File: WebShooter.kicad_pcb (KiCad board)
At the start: 2 copper layers, 60 x 46 mm, 29 parts, among them J1 ESP32_LEFT, J2 ESP32_RIGHT, Q1 AO3400A, U1 AMS1117-3.3

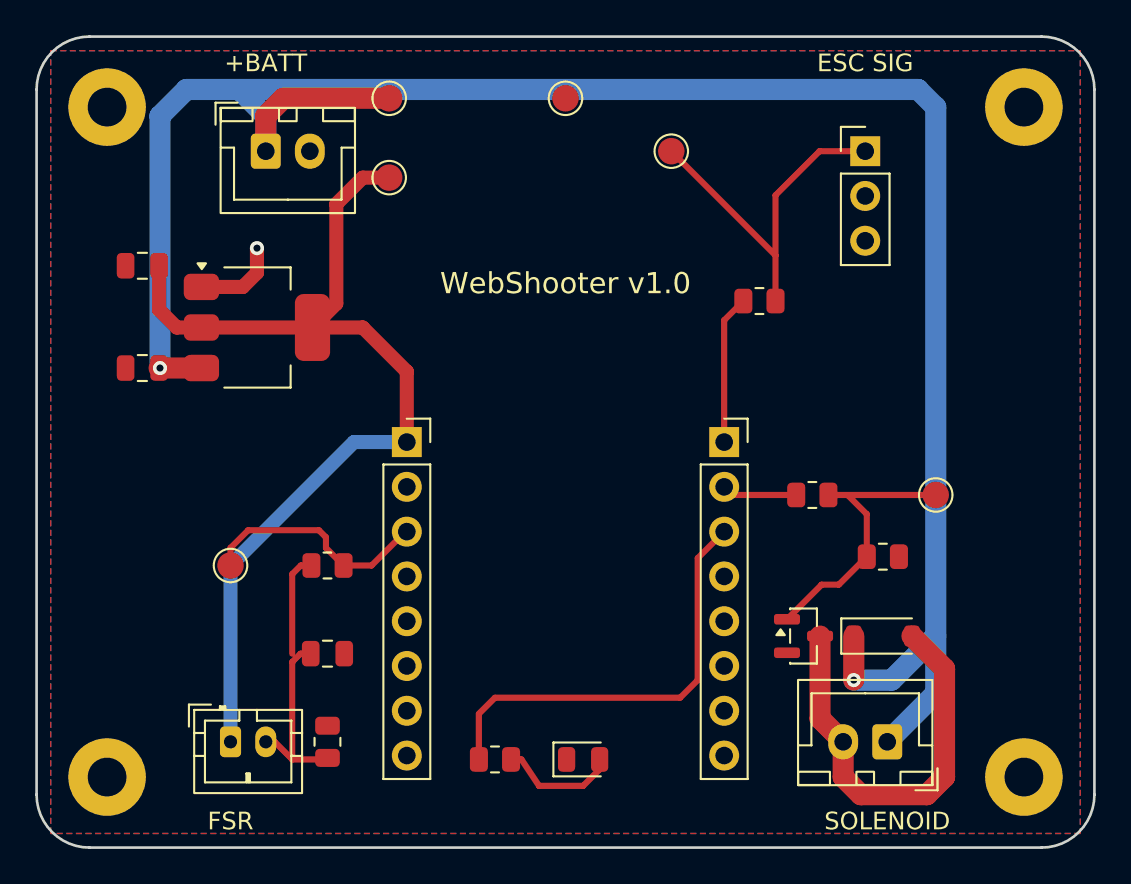
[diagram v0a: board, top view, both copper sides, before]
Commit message: feat: Redesign ultra-compact 38x38mm PCB, 0 DRC violations, 45deg routing & add 3D case CAD
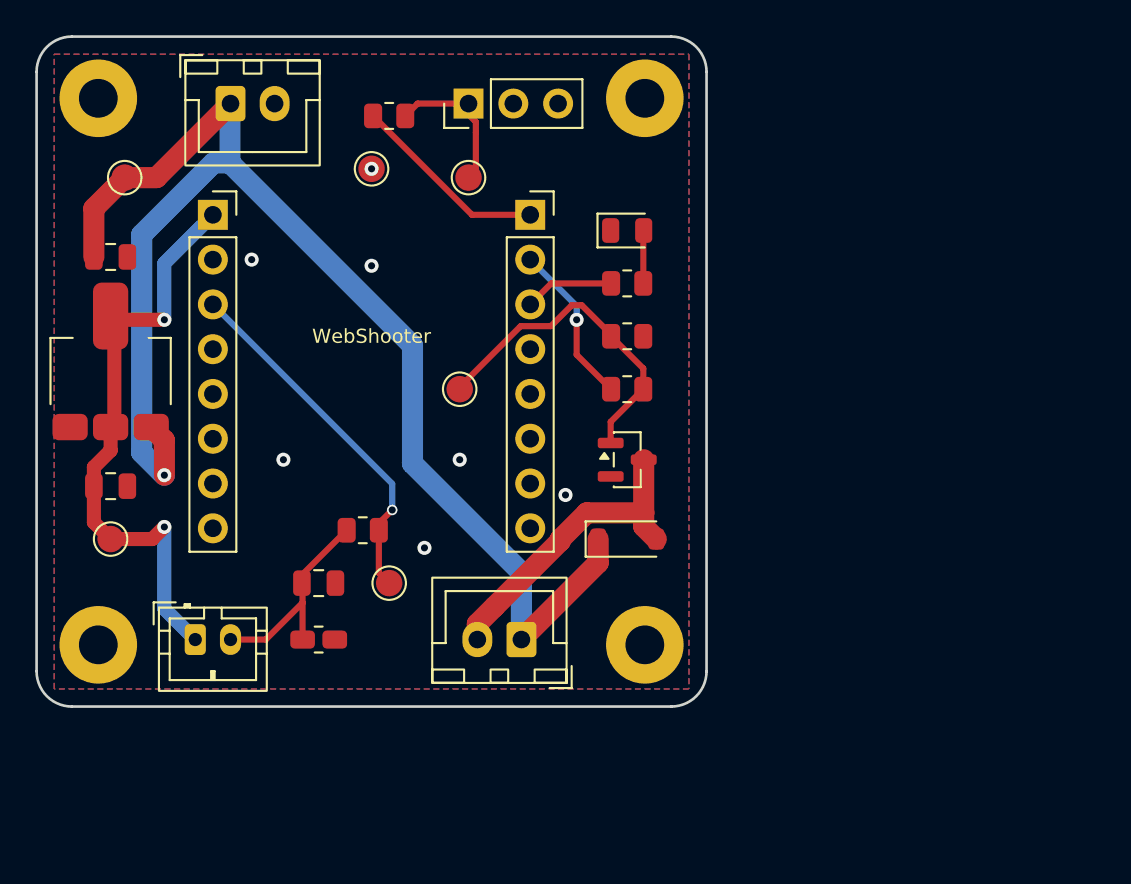
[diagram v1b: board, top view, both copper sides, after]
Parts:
- moved D2 30.1 mm to (133.5, 111.0)
- moved R_LED 28.0 mm to (133.5, 114.0)
- moved TP_GATE 27.7 mm to (124.0, 120.0)
- moved TP_3V3 25.9 mm to (104.2, 128.5)
- moved R_PWM 23.5 mm to (120.0, 104.5)
- moved H4 22.8 mm to (134.5, 134.5)
- moved J_ESC 22.7 mm to (124.5, 103.8), turned to 90 degrees
- moved J_SOL 21.5 mm to (127.5, 134.2)
- moved H2 21.5 mm to (134.5, 103.5)
- moved R_PD 19.1 mm to (133.5, 117.0)
- moved J1 16.9 mm to (110.0, 110.1)
- moved J2 16.9 mm to (128.0, 110.1)
- moved TP_VBATT 15.7 mm to (105.0, 108.0)
- moved D1 15.5 mm to (133.5, 128.5)
- moved Q1 14.1 mm to (133.5, 124.0)
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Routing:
- net +BATT: track 120.6 -> 81.6 mm, vias 2 -> 1
- net +3.3V: track 56.1 -> 34.0 mm, vias 0 -> 2
- net LED_STAT: track 24.8 -> 5.08 mm
- net ESC_PWM: track 20.5 -> 8.68 mm
- net FSR_ADC: track 13.4 -> 20.6 mm, vias 0 -> 1
- net SOL_DRAIN: track 23.9 -> 17.8 mm
- net MCU_GATE: track 4.28 -> 9.25 mm, vias 0 -> 1
- net GND: track 4.88 -> 0.00 mm, vias 1 -> 7
- net FSR_IN: track 16.6 -> 12.2 mm
- net LED_A: track 6.78 -> 3.01 mm
- net SOL_GATE: track 16.0 -> 19.0 mm
- net MCU_PWM: track 8.45 -> 11.2 mm
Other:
- board size 60 x 46 mm -> 38 x 38 mm
- board text added: "WebShooter"
- board text removed: "+BATT"
- board text removed: "ESC SIG"
- board text removed: "FSR"
- board text removed: "SOLENOID"
- board text removed: "WebShooter v1.0"
